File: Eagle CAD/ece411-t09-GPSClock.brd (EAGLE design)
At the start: 59.4 x 74 mm, 52 parts, among them IC3 LM1117, J1 AMP FCI 10103594-0001LF, J2 ISP, J3 POWER_JACKSUPER_BOMB_DIGITY, J4 BM06B-SRSS-TB, Q1 1A/60V/500mΩ, U1 CH340C, U2 LIGHT_SENSORALS, U3 AP2112-3.3V, U4 ATMEGA328P_TQFP, U5 1571984-1, Y1 16MHz

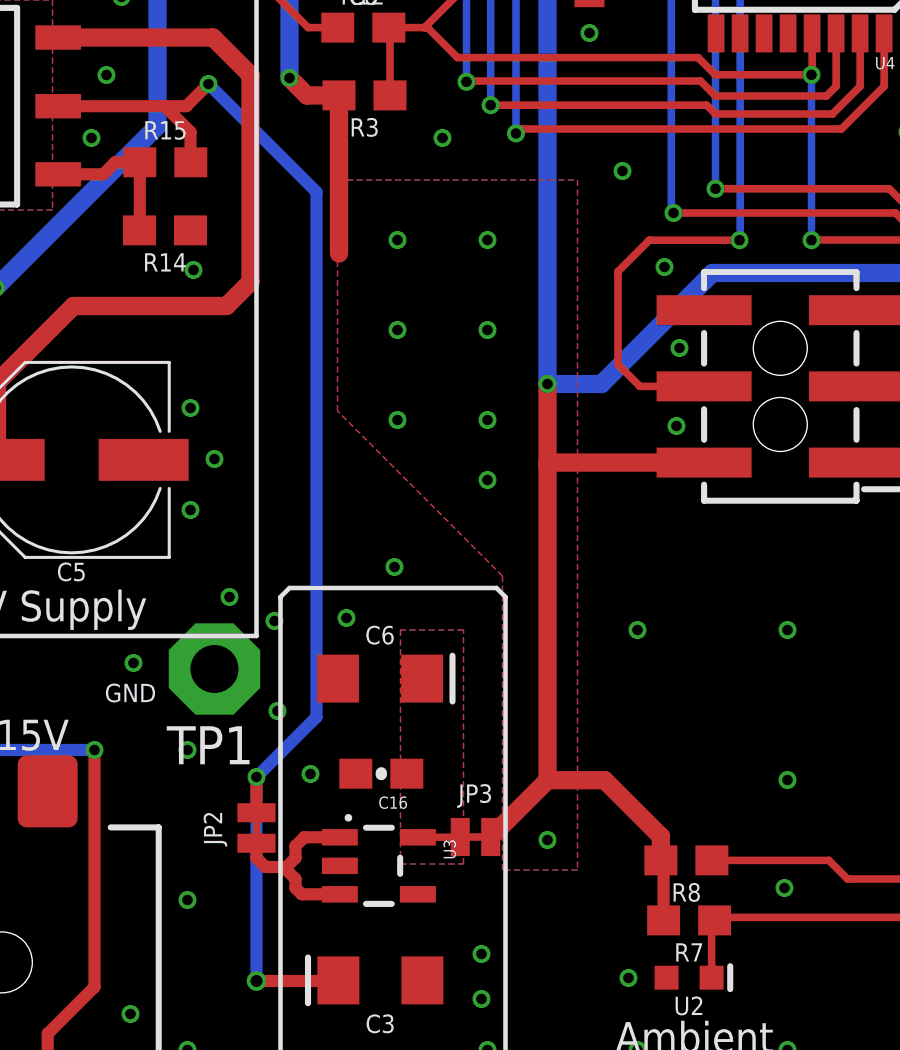
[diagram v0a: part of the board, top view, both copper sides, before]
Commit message: Stitched the N$7 (3.3V) plane
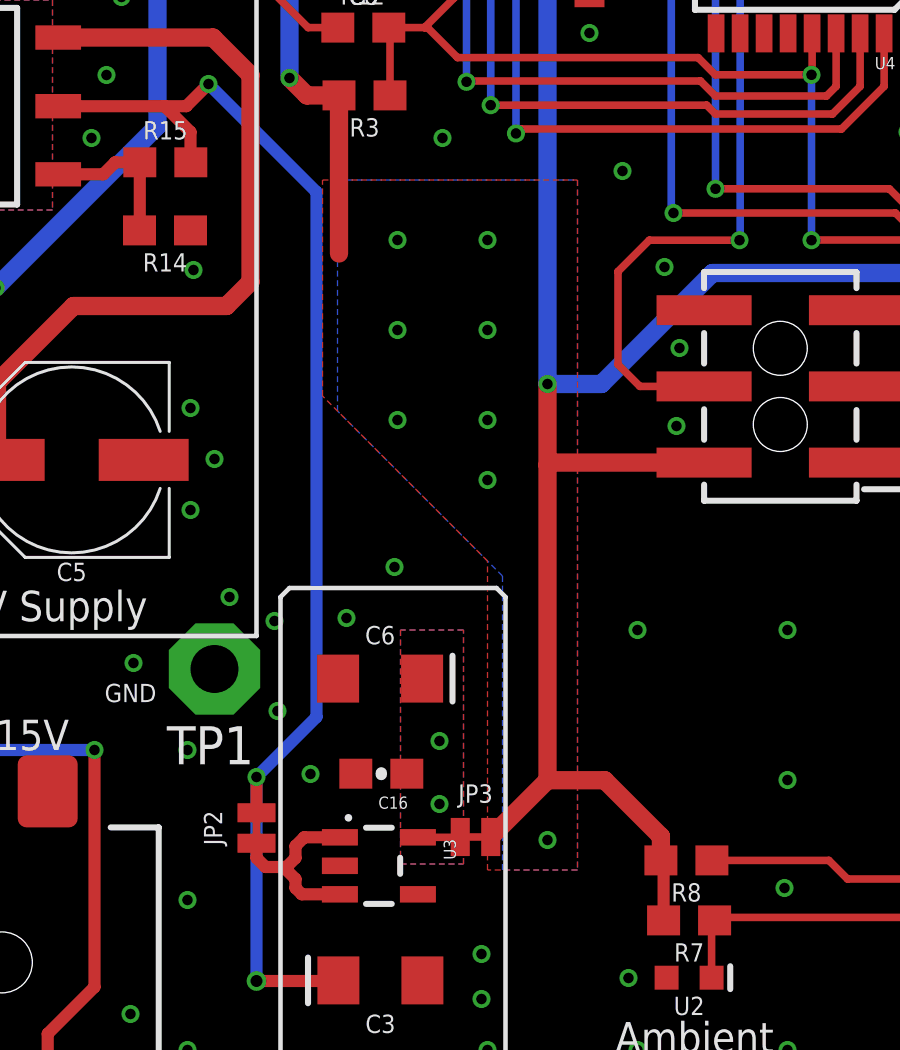
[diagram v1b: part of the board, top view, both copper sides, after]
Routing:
- net N$7: vias 0 -> 2
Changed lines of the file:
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@@
 <wire x1="41.1" y1="43.2" x2="43.1" y2="41.2" width="0.6096" layer="16"/>
 <contactref element="R7" pad="2"/>
-<polygon width="0.6096" layer="1">
-<vertex x="25.5" y="11"/>
-<vertex x="25.5" y="20.8"/>
-<vertex x="20" y="26.3"/>
-<vertex x="20" y="34"/>
+<polygon width="0.254" layer="1">
+<vertex x="25" y="11"/>
+<vertex x="25" y="21.3"/>
+<vertex x="19.5" y="26.8"/>
+<vertex x="19.5" y="34"/>
 <vertex x="28" y="34"/>
 <vertex x="28" y="11"/>
 </polygon>
-<polygon width="0.6096" layer="16">
+<polygon width="0.254" layer="16">
 <vertex x="25.5" y="11"/>
 <vertex x="25.5" y="20.8"/>
@@
 <wire x1="24.092" y1="12.1" x2="24.082" y2="12.09" width="0.254" layer="1"/>
 <wire x1="24.082" y1="12.09" x2="22.6801" y2="12.09" width="0.254" layer="1"/>
+<via x="23.4" y="13.2" extent="1-16" drill="0.35"/>
+<via x="23.4" y="15.3" extent="1-16" drill="0.35"/>
 </signal>
 <signal name="N$8">
